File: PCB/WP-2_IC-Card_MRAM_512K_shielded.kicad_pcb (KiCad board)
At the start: 2 copper layers, 54 x 54 mm, 39 parts, among them J1 SMS-138-01-G-S, SW1 CUS-14TB, U1 MR2A08xxYSxxx, U2 MIC5317-3.3YD5, U3 4245, U4 4245, U5 4245, U6 4245

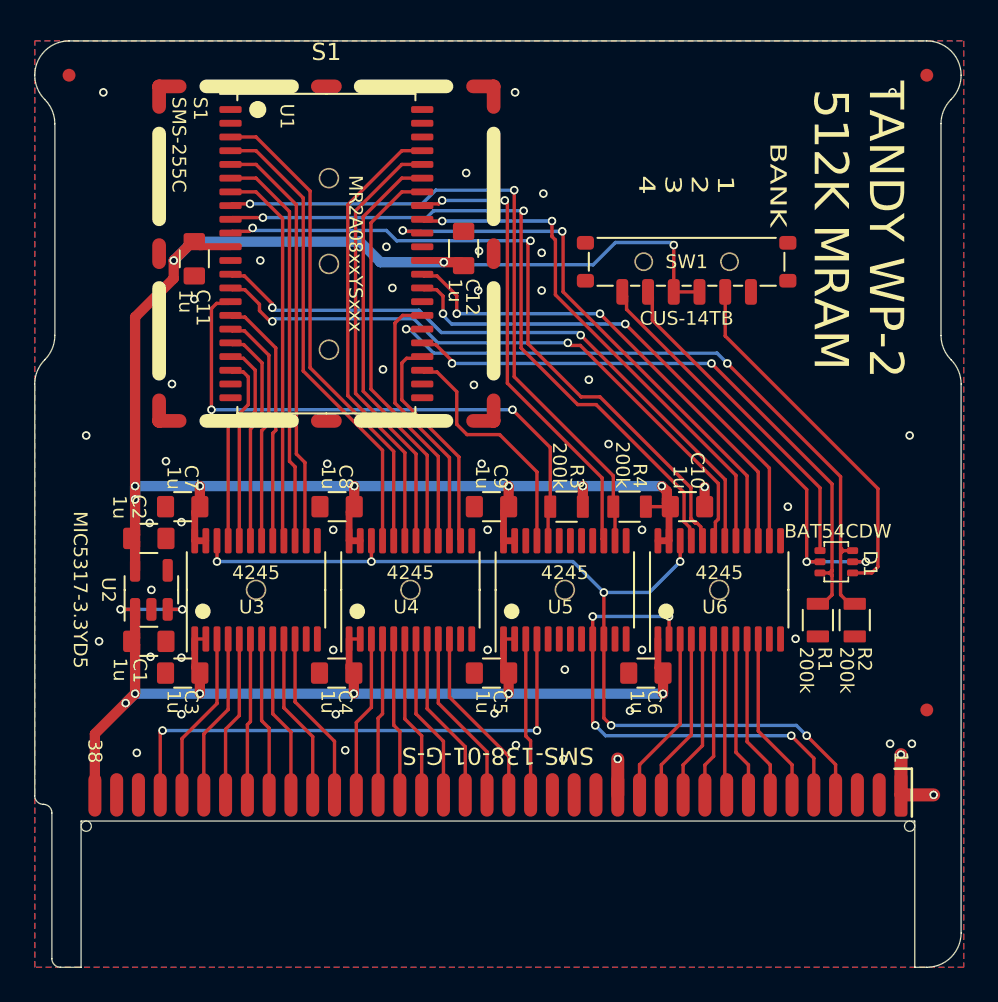
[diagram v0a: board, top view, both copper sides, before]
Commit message: cleanup names, cover inside corner reliefs
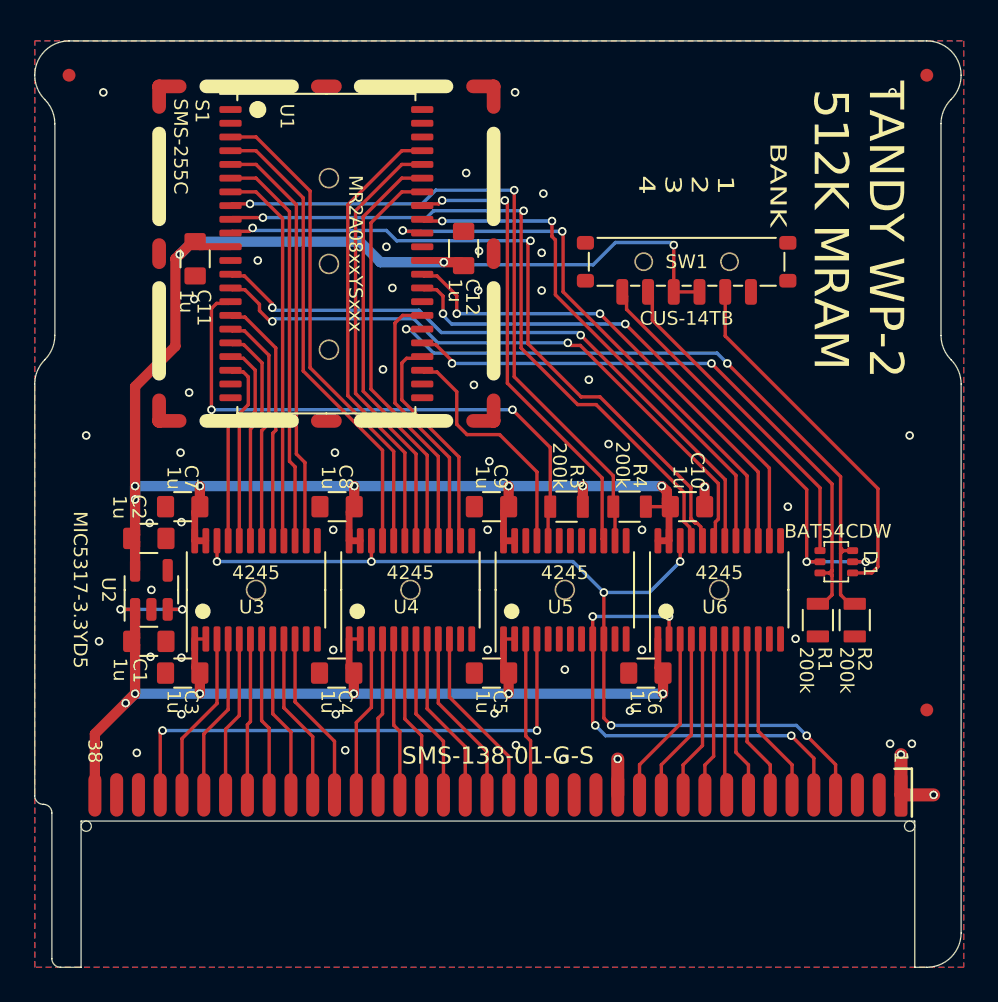
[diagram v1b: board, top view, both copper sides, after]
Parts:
- N1: footprint 000_LOCAL:WP-2_IC_Card_Cover_MRAM_512 -> 000_LOCAL:WP-2_IC-Card_Cover_MRAM_512
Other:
- board text added: "Just an idea in progress to use a steel RF shield as a magnetic shield to protect the MRAM. Unknown how much this kind of RF shield would actually help. * steel instead of mu-metal * single layer * vent holes * bottom wide open But it probably doesn't hurt at least."

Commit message: better can for shielded mram
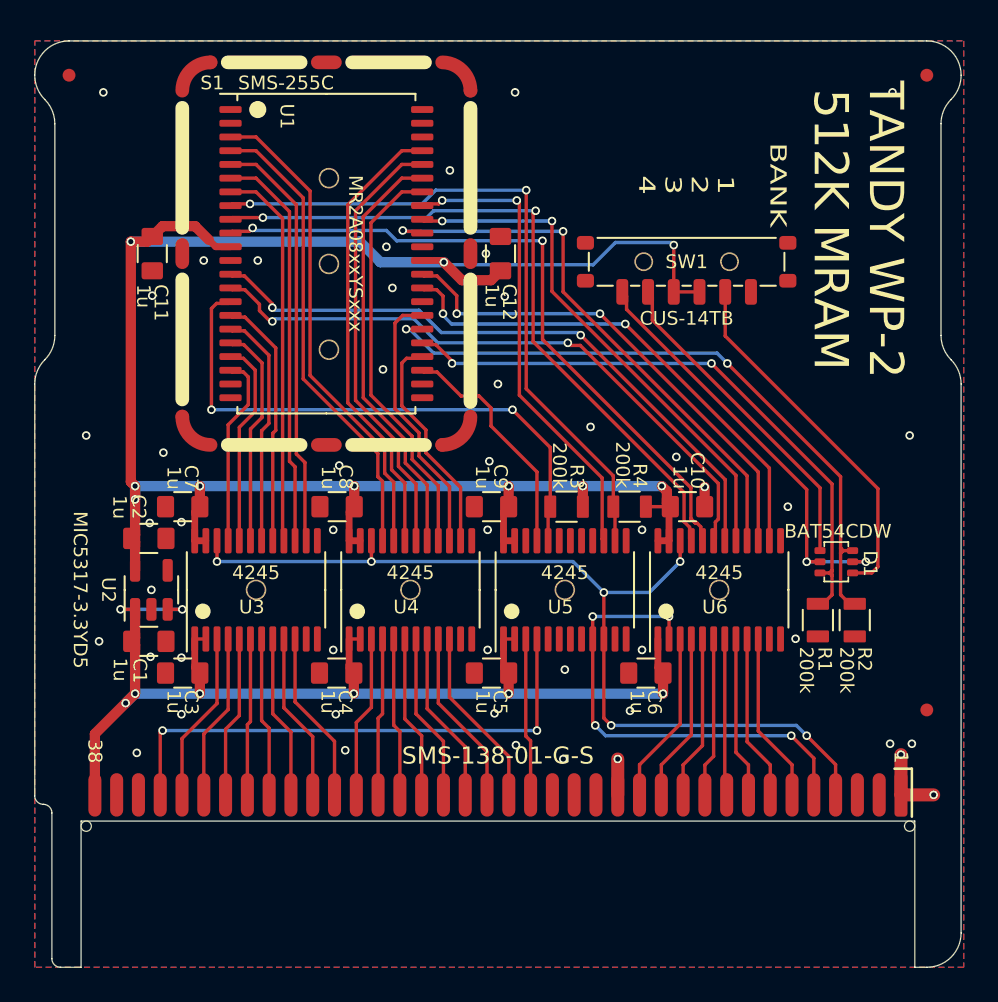
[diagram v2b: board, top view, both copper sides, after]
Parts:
- S1: footprint 000_LOCAL:SMS-255C -> 000_LOCAL:MS226-10S
- moved C11 2.52 mm to (115.8, 80.6)
- moved C12 2.17 mm to (136.1, 80.6)
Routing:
- net VMEM: track 110.2 -> 118.5 mm
- net GND: vias 52 -> 49
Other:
- board text added: "Just an idea in progress to use a steel RF shield as a magnetic shield to protect the MRAM. Unknown how much this kind of RF shield would actually help, with the bottom still open for instanvce, but it probably doesn't hurt at least."
- board text removed: "Just an idea in progress to use a steel RF shield as a magnetic shield to protect the MRAM. Unknown how much this kind of RF shield would actually help. * steel instead of mu-metal * single layer * vent holes * bottom wide open But it probably doesn't hurt at least."

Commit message: redraw board outline and copy to all boards
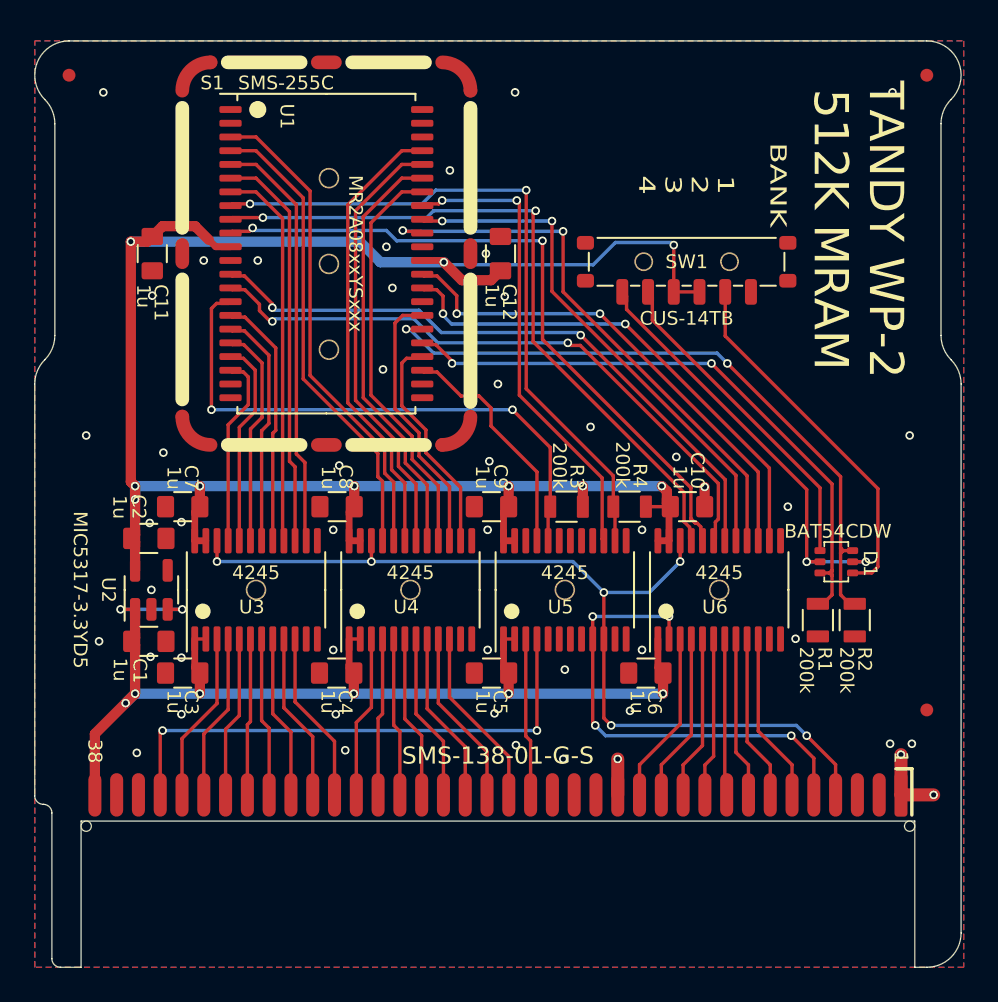
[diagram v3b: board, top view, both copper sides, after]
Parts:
- removed the REF** at (160.9, 70.2)
- removed the REF** at (111.0, 70.2)
- removed the REF** at (160.9, 107.2)
- added REF**: Fiducial_1.5, 000_LOCAL:Fiducial_1.5, F.Cu at (160.9, 70.2)
- added REF**: Fiducial_1.5, 000_LOCAL:Fiducial_1.5, F.Cu at (160.9, 107.2)
- added REF**: Fiducial_1.5, 000_LOCAL:Fiducial_1.5, F.Cu at (111.0, 70.2)
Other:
- outline, holes or cut-outs redrawn

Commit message: rom wren sw, boms, footprints, shielded mram
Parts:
- C1, C10, C11, C12, C2, C3, C4, C5, C6, C7, C8, C9: footprint 000_LOCAL:C_0805_1mm -> 000_LOCAL:C_0805
- S1: value SMS-255C -> MS226-10S
- moved C3 0.15 mm to (117.6, 105.2)
- moved C4 0.15 mm to (126.5, 105.2)
- moved C5 0.15 mm to (135.6, 105.2)
- moved C6 0.15 mm to (144.6, 105.2)
- moved C10 0.15 mm to (147.0, 95.2)
- moved C7 0.15 mm to (117.6, 95.2)
- moved C8 0.15 mm to (126.6, 95.2)
- moved C9 0.15 mm to (135.6, 95.2)
- moved R3 0.15 mm to (139.9, 95.2)
- moved R4 0.15 mm to (143.6, 95.2)
- moved C2 0.10 mm to (115.6, 97.1)
- moved C1 0.10 mm to (115.6, 103.3)
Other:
- board text added: "Just an idea in progress to use a steel RF shield as a magnetic shield to protect the MRAM. Unknown how much this kind of RF shield would actually help, with the bottom still open for instance, but it probably doesn't hurt at least. Set mram_shield = true; in WP-2_Card_Cover.scad"
- board text removed: "Just an idea in progress to use a steel RF shield as a magnetic shield to protect the MRAM. Unknown how much this kind of RF shield would actually help, with the bottom still open for instanvce, but it probably doesn't hurt at least."

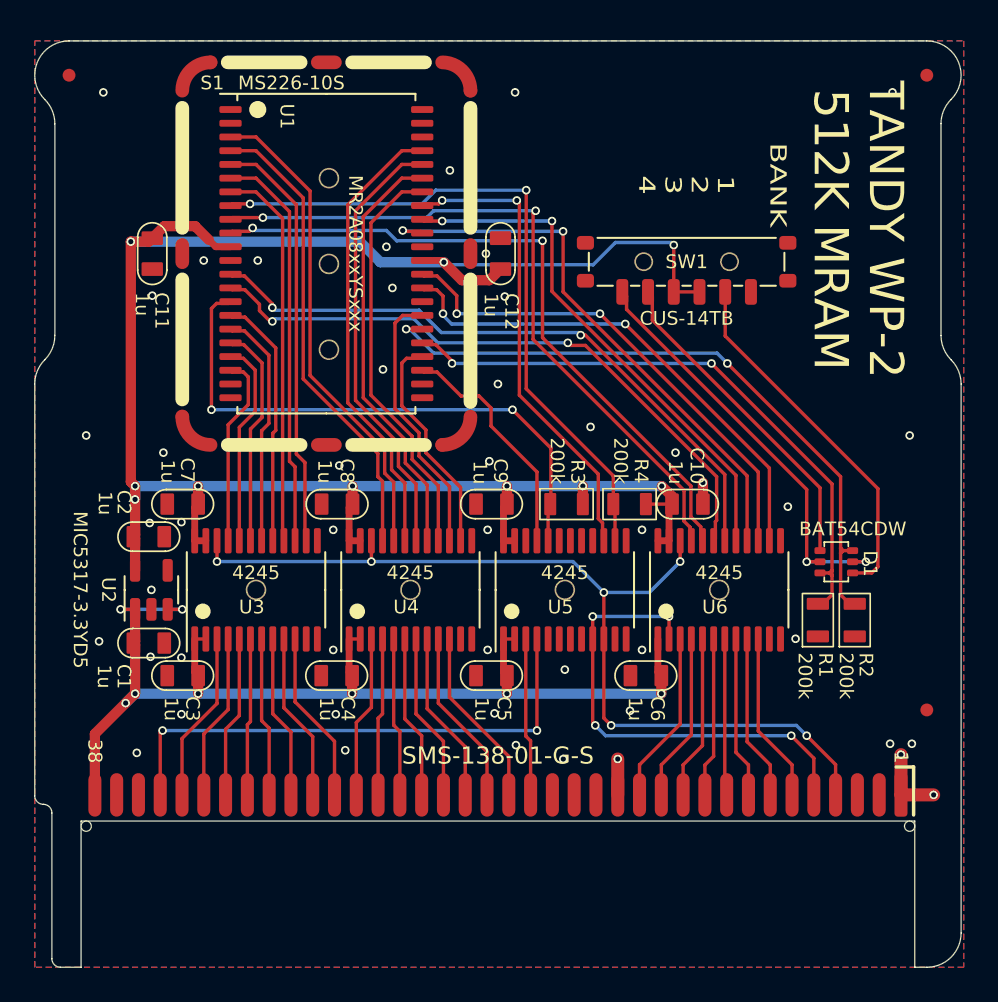
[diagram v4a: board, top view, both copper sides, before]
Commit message: MRAM card that supports both 128K and 512K, and supports emulating rom
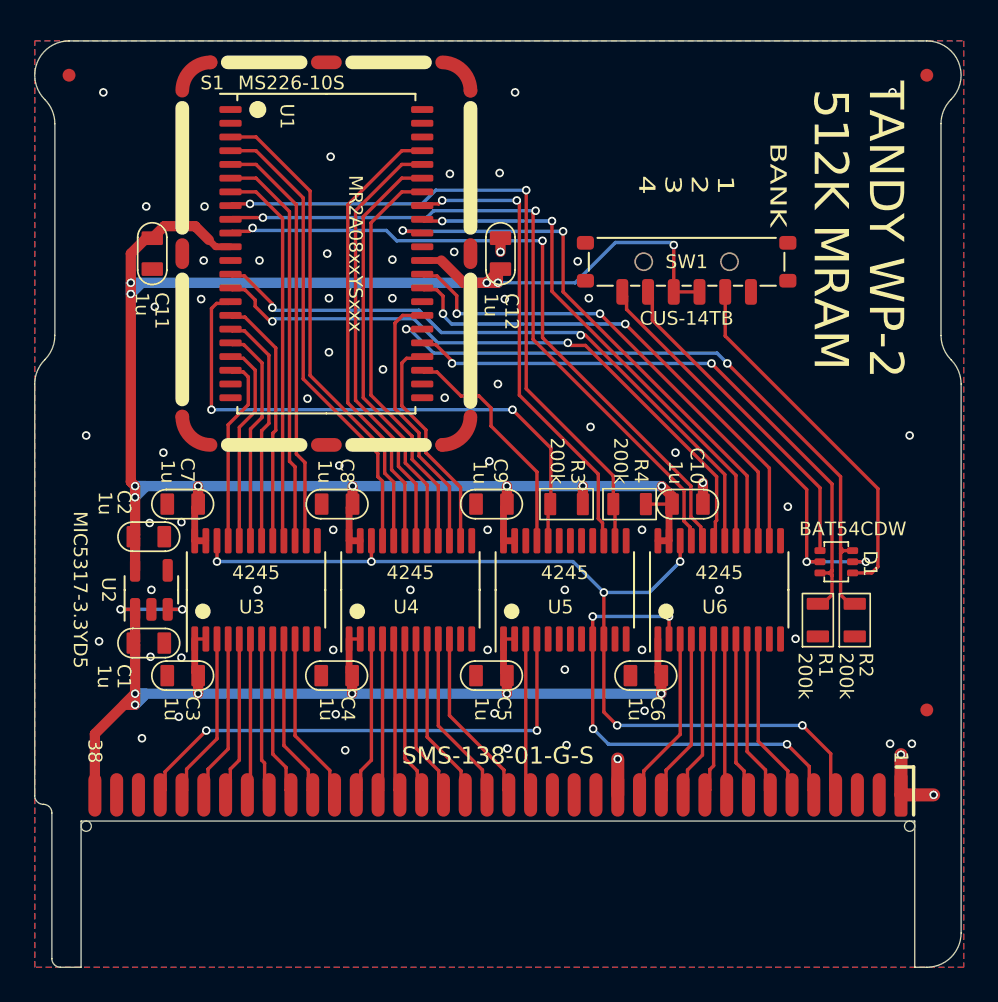
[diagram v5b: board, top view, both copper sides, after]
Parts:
- removed the REF** at (130.8, 100.2)
- removed the REF** at (126.1, 76.2)
- removed the REF** at (121.8, 100.2)
- removed the REF** at (126.1, 86.2)
- removed the REF** at (148.8, 100.2)
- removed the REF** at (139.8, 100.2)
- removed the REF** at (126.1, 81.2)
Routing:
- net /~{WE}: track 31.0 -> 29.5 mm
- net VMEM: track 118.4 -> 117.2 mm, vias 10 -> 12
- net GND: track 7.59 -> 8.39 mm, vias 49 -> 66
- net VBUS: track 63.6 -> 62.9 mm

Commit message: silkscreens, board outlines, switch slider, covers fitment, copper to edge
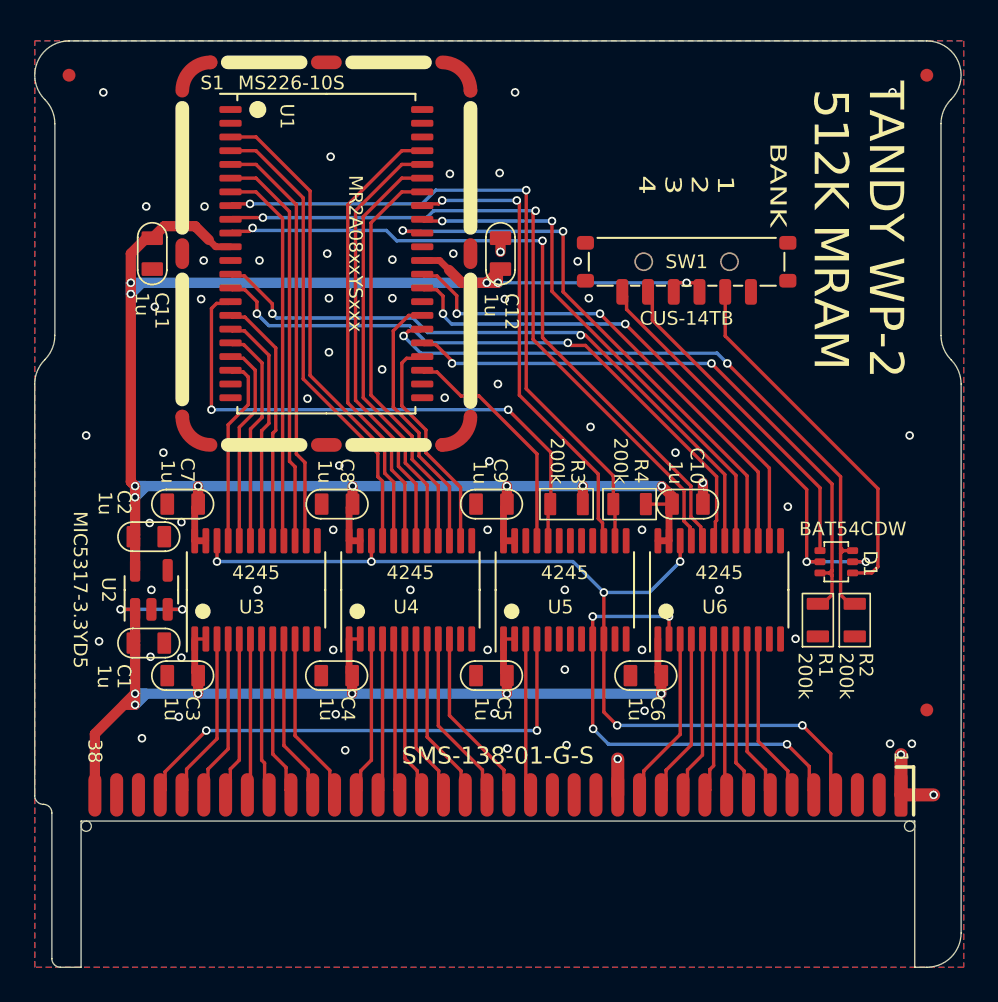
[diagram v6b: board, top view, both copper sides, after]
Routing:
- net VMEM: track 117.2 -> 115.2 mm
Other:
- board text added: "Just an idea in progress to use a steel EMI/RF shield to try to protect the MRAM from magnetic fields. Unknown how much this kind of shield would actually help. The shield is thin steel, when what you want is thick mumetal. Set mram_shield = true; in WP-2_Card_Cover.scad"
- board text removed: "Just an idea in progress to use a steel RF shield as a magnetic shield to protect the MRAM. Unknown how much this kind of RF shield would actually help, with the bottom still open for instance, but it probably doesn't hurt at least. Set mram_shield = true; in WP-2_Card_Cover.scad"
